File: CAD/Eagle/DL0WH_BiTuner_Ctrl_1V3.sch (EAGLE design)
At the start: 157 parts, among them Q0321 ABS07-32.768KHZ, U0101 STM32L476RXT_64PIN_LDO, U0601 MC33996, U0701 MC33996, U0801 MC33996, U0921 TS5A23166, U0941 LM2611, U0951 OPA354, U0961 OPA354, U0962 MCP4661-103E-MS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

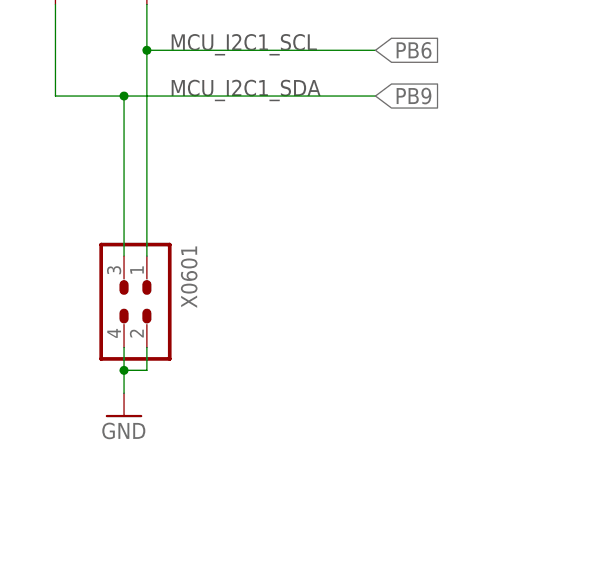
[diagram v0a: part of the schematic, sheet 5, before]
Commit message: HW_1V3 - CAD/Eagle - Rename X0601 to X0501
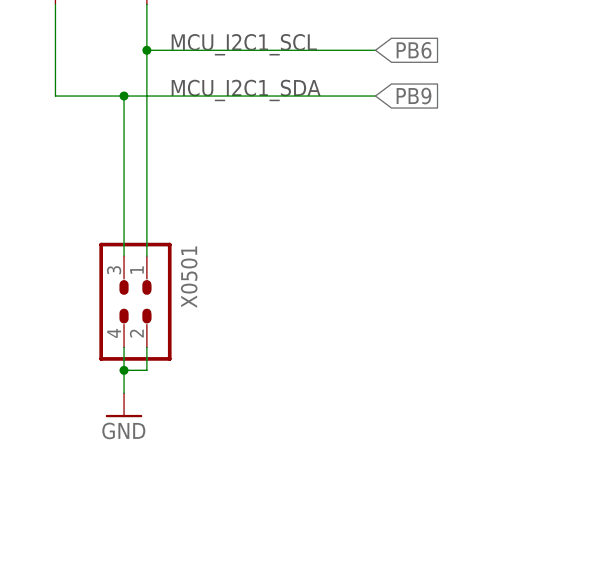
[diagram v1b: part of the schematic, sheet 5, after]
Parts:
- renumbered X0601 to X0501
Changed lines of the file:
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@@
 <part name="R0971" library="df4iah_rcl" deviceset="R-EU_" device="R0402" value="10kR"/>
 <part name="GND0961" library="df4iah_supply" deviceset="GND" device=""/>
-<part name="X0601" library="df4iah_connector" deviceset="HEADER-2X2" device=""/>
+<part name="X0501" library="df4iah_connector" deviceset="HEADER-2X2" device=""/>
 <part name="GND0501" library="df4iah_supply" deviceset="GND" device=""/>
 <part name="+3V6" library="df4iah_supply" deviceset="+3V3" device=""/>
@@
 <instance part="R0511" gate="G$1" x="22.86" y="134.62" rot="R90"/>
 <instance part="R0512" gate="G$1" x="33.02" y="134.62" rot="R90"/>
-<instance part="X0601" gate="G$1" x="33.02" y="96.52" rot="R270"/>
+<instance part="X0501" gate="G$1" x="33.02" y="96.52" rot="R270"/>
 <instance part="GND0501" gate="1" x="30.48" y="83.82"/>
 </instances>
@@
 <pinref part="R0512" gate="G$1" pin="1"/>
 <wire x1="33.02" y1="124.46" x2="33.02" y2="129.54" width="0.1524" layer="91"/>
-<pinref part="X0601" gate="G$1" pin="1"/>
+<pinref part="X0501" gate="G$1" pin="1"/>
 <wire x1="33.02" y1="124.46" x2="33.02" y2="101.6" width="0.1524" layer="91"/>
 <junction x="33.02" y="124.46"/>
@@
 <wire x1="30.48" y1="119.38" x2="58.42" y2="119.38" width="0.1524" layer="91"/>
 <wire x1="22.86" y1="119.38" x2="22.86" y2="129.54" width="0.1524" layer="91"/>
-<pinref part="X0601" gate="G$1" pin="3"/>
+<pinref part="X0501" gate="G$1" pin="3"/>
 <wire x1="30.48" y1="119.38" x2="30.48" y2="101.6" width="0.1524" layer="91"/>
 <junction x="30.48" y="119.38"/>
@@
 <net name="GND" class="0">
 <segment>
-<pinref part="X0601" gate="G$1" pin="2"/>
+<pinref part="X0501" gate="G$1" pin="2"/>
 <wire x1="33.02" y1="91.44" x2="33.02" y2="88.9" width="0.1524" layer="91"/>
-<pinref part="X0601" gate="G$1" pin="4"/>
+<pinref part="X0501" gate="G$1" pin="4"/>
 <wire x1="30.48" y1="91.44" x2="30.48" y2="88.9" width="0.1524" layer="91"/>
 <wire x1="33.02" y1="88.9" x2="30.48" y2="88.9" width="0.1524" layer="91"/>

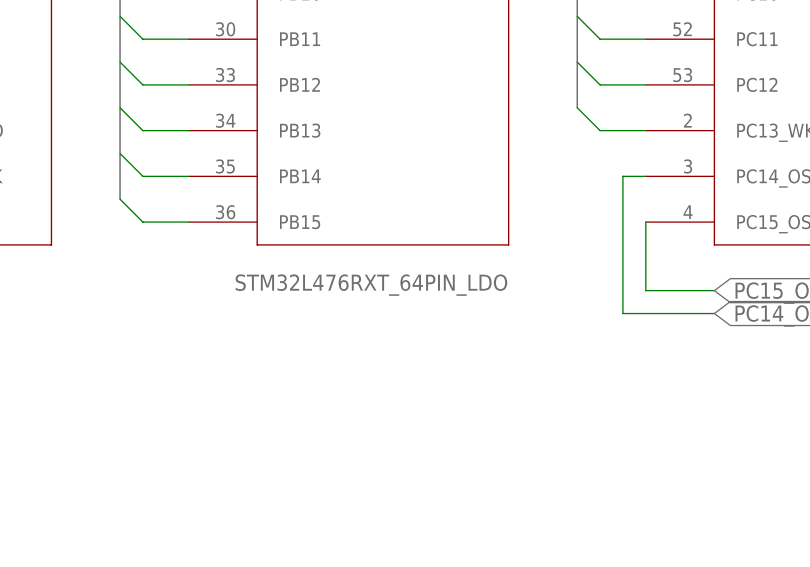
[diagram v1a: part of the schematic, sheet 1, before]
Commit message: HW_1V3 - CAD/Eagle - MCU name fixed
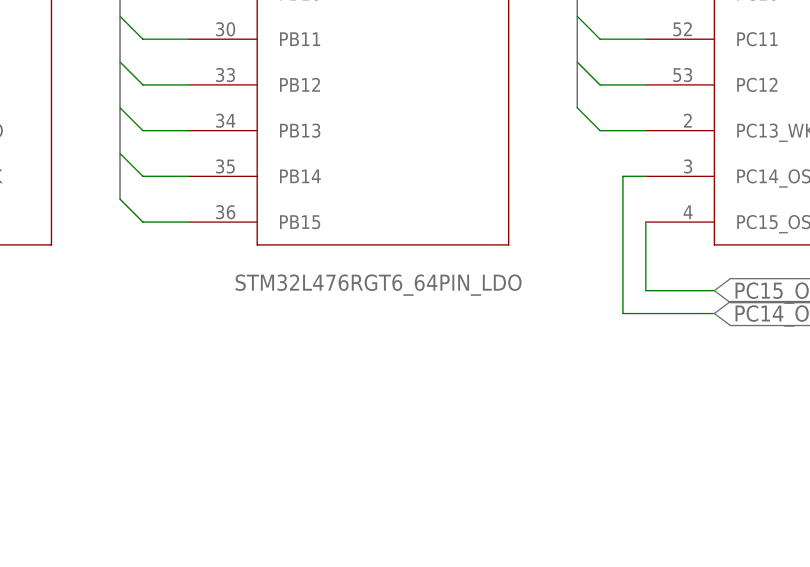
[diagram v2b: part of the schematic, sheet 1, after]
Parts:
- U0101: value STM32L476RXT_64PIN_LDO -> STM32L476RGT6_64PIN_LDO
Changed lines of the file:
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@@
 <part name="C1223" library="df4iah_rcl" deviceset="C-EU" device="C0603" value="22uF"/>
 <part name="X1211" library="df4iah_connector" deviceset="WIRE-TO-BOARD_5MM08_1X02" device=""/>
-<part name="U0101" library="df4iah_stm32l4" deviceset="STM32L476RXT_64PIN_LDO" device=""/>
+<part name="U0101" library="df4iah_stm32l4" deviceset="STM32L476RXT_64PIN_LDO" device="" value="STM32L476RGT6_64PIN_LDO"/>
 <part name="FRAME_07" library="df4iah_frame" deviceset="A4L-LOC" device="" value="Holes"/>
 <part name="FRAME_08" library="df4iah_frame" deviceset="A4L-LOC" device="" value="Holes"/>

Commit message: HW_1V3 - CAD/Eagle - renaming fix, jumper replaced by 0R bridge
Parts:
- removed C0054: 10nF, df4iah_rcl:C-EUC0603
- removed SJ0401: (no value), df4iah_jumper:SJ
- added C1054: 10nF, df4iah_rcl:C-EUC0402
- added R0401: 0R, df4iah_rcl:R-EU_R0402
- C0942: device df4iah_rcl:C-EUC0805 -> df4iah_rcl:C-EUC0603
- C1051, C1052, C1053, C1151, C1152, C1153, C1154: device df4iah_rcl:C-EUC0603 -> df4iah_rcl:C-EUC0402
- R0962: value 1.0kR -> 1kR
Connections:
- net +3V3: now also R0401.1; no longer SJ0401.1
- net GND: now also C1054.2; no longer C0054.2
- net MCU_VDD: now also R0401.2; no longer SJ0401.2
- net RS_DTE_RTR: now also C1054.1; no longer C0054.1
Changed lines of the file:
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@@
 <part name="C0412" library="df4iah_rcl" deviceset="C-EU" device="C0402" value="10nF"/>
 <part name="GND0411" library="df4iah_supply" deviceset="GND" device=""/>
-<part name="SJ0401" library="df4iah_jumper" deviceset="SJ" device=""/>
+<part name="R0401" library="df4iah_rcl" deviceset="R-EU_" device="R0402" value="0R"/>
 <part name="GND0201" library="df4iah_supply" deviceset="GND" device=""/>
 <part name="X0222" library="df4iah_connector" deviceset="HEADER-1X2" device=""/>
@@
 <part name="R0901" library="df4iah_rcl" deviceset="R-EU_" device="R0402" value="1kR"/>
 <part name="R0911" library="df4iah_rcl" deviceset="R-EU_" device="R0402" value="1kR"/>
-<part name="C1052" library="df4iah_rcl" deviceset="C-EU" device="C0603" value="10nF"/>
-<part name="C1051" library="df4iah_rcl" deviceset="C-EU" device="C0603" value="10nF"/>
-<part name="C1053" library="df4iah_rcl" deviceset="C-EU" device="C0603" value="10nF"/>
-<part name="C0054" library="df4iah_rcl" deviceset="C-EU" device="C0603" value="10nF"/>
+<part name="C1052" library="df4iah_rcl" deviceset="C-EU" device="C0402" value="10nF"/>
+<part name="C1051" library="df4iah_rcl" deviceset="C-EU" device="C0402" value="10nF"/>
+<part name="C1053" library="df4iah_rcl" deviceset="C-EU" device="C0402" value="10nF"/>
+<part name="C1054" library="df4iah_rcl" deviceset="C-EU" device="C0402" value="10nF"/>
 <part name="GND0001" library="df4iah_supply" deviceset="GND" device=""/>
 <part name="GND0002" library="df4iah_supply" deviceset="GND" device=""/>
-<part name="C1152" library="df4iah_rcl" deviceset="C-EU" device="C0603" value="10nF"/>
-<part name="C1151" library="df4iah_rcl" deviceset="C-EU" device="C0603" value="10nF"/>
-<part name="C1153" library="df4iah_rcl" deviceset="C-EU" device="C0603" value="10nF"/>
-<part name="C1154" library="df4iah_rcl" deviceset="C-EU" device="C0603" value="10nF"/>
+<part name="C1152" library="df4iah_rcl" deviceset="C-EU" device="C0402" value="10nF"/>
+<part name="C1151" library="df4iah_rcl" deviceset="C-EU" device="C0402" value="10nF"/>
+<part name="C1153" library="df4iah_rcl" deviceset="C-EU" device="C0402" value="10nF"/>
+<part name="C1154" library="df4iah_rcl" deviceset="C-EU" device="C0402" value="10nF"/>
 <part name="GND0005" library="df4iah_supply" deviceset="GND" device=""/>
 <part name="GND0006" library="df4iah_supply" deviceset="GND" device=""/>
@@
 <part name="U0961" library="df4iah_opamp" deviceset="OPA354" device=""/>
 <part name="R0961" library="df4iah_rcl" deviceset="R-EU_" device="R0402" value="1kR"/>
-<part name="R0962" library="df4iah_rcl" deviceset="R-EU_" device="R0402" value="1.0kR"/>
+<part name="R0962" library="df4iah_rcl" deviceset="R-EU_" device="R0402" value="1kR"/>
 <part name="R0963" library="df4iah_rcl" deviceset="R-EU_" device="R0402" value="10kR"/>
 <part name="C0963" library="df4iah_rcl" deviceset="C-EU" device="C0402" value="100pF"/>
@@
 <part name="GND0941" library="df4iah_supply" deviceset="GND" device=""/>
 <part name="L0941" library="df4iah_rcl" deviceset="L-EU" device="L1812" value="20uH"/>
-<part name="C0942" library="df4iah_rcl" deviceset="C-EU" device="C0805" value="2.2uF"/>
+<part name="C0942" library="df4iah_rcl" deviceset="C-EU" device="C0603" value="2.2uF"/>
 <part name="GND0942" library="df4iah_supply" deviceset="GND" device=""/>
 <part name="L0943" library="df4iah_rcl" deviceset="L-EU" device="L1812" value="20uH"/>
@@
 <instance part="C0412" gate="G$1" x="200.66" y="101.6"/>
 <instance part="GND0411" gate="1" x="200.66" y="88.9"/>
-<instance part="SJ0401" gate="1" x="119.38" y="147.32"/>
+<instance part="R0401" gate="G$1" x="119.38" y="147.32"/>
 <instance part="GND0441" gate="1" x="200.66" y="33.02"/>
 <instance part="R0441" gate="G$1" x="213.36" y="38.1"/>
@@
 <wire x1="165.1" y1="147.32" x2="165.1" y2="139.7" width="0.1524" layer="91"/>
 <junction x="165.1" y="147.32"/>
-<pinref part="SJ0401" gate="1" pin="2"/>
+<pinref part="R0401" gate="G$1" pin="2"/>
 <wire x1="134.62" y1="147.32" x2="124.46" y2="147.32" width="0.1524" layer="91"/>
 <pinref part="C0410" gate="G$1" pin="1"/>
@@
 <net name="+3V3" class="0">
 <segment>
-<pinref part="SJ0401" gate="1" pin="1"/>
+<pinref part="R0401" gate="G$1" pin="1"/>
 <label x="40.64" y="147.32" size="1.778" layer="95" rot="R180" xref="yes"/>
 <wire x1="114.3" y1="147.32" x2="40.64" y2="147.32" width="0.1524" layer="91"/>
@@
 <instance part="C1051" gate="G$1" x="180.34" y="114.3"/>
 <instance part="C1053" gate="G$1" x="180.34" y="81.28"/>
-<instance part="C0054" gate="G$1" x="193.04" y="81.28"/>
+<instance part="C1054" gate="G$1" x="193.04" y="81.28"/>
 <instance part="GND0001" gate="1" x="180.34" y="106.68"/>
 <instance part="GND0002" gate="1" x="180.34" y="73.66"/>
@@
 <wire x1="180.34" y1="76.2" x2="193.04" y2="76.2" width="0.1524" layer="91"/>
 <junction x="180.34" y="76.2"/>
-<pinref part="C0054" gate="G$1" pin="2"/>
+<pinref part="C1054" gate="G$1" pin="2"/>
 </segment>
 </net>
@@
 <pinref part="X1053" gate="G$1" pin="2"/>
 <wire x1="165.1" y1="88.9" x2="193.04" y2="88.9" width="0.1524" layer="91"/>
-<pinref part="C0054" gate="G$1" pin="1"/>
+<pinref part="C1054" gate="G$1" pin="1"/>
 <wire x1="193.04" y1="88.9" x2="215.9" y2="88.9" width="0.1524" layer="91"/>
 <wire x1="193.04" y1="88.9" x2="193.04" y2="83.82" width="0.1524" layer="91"/>

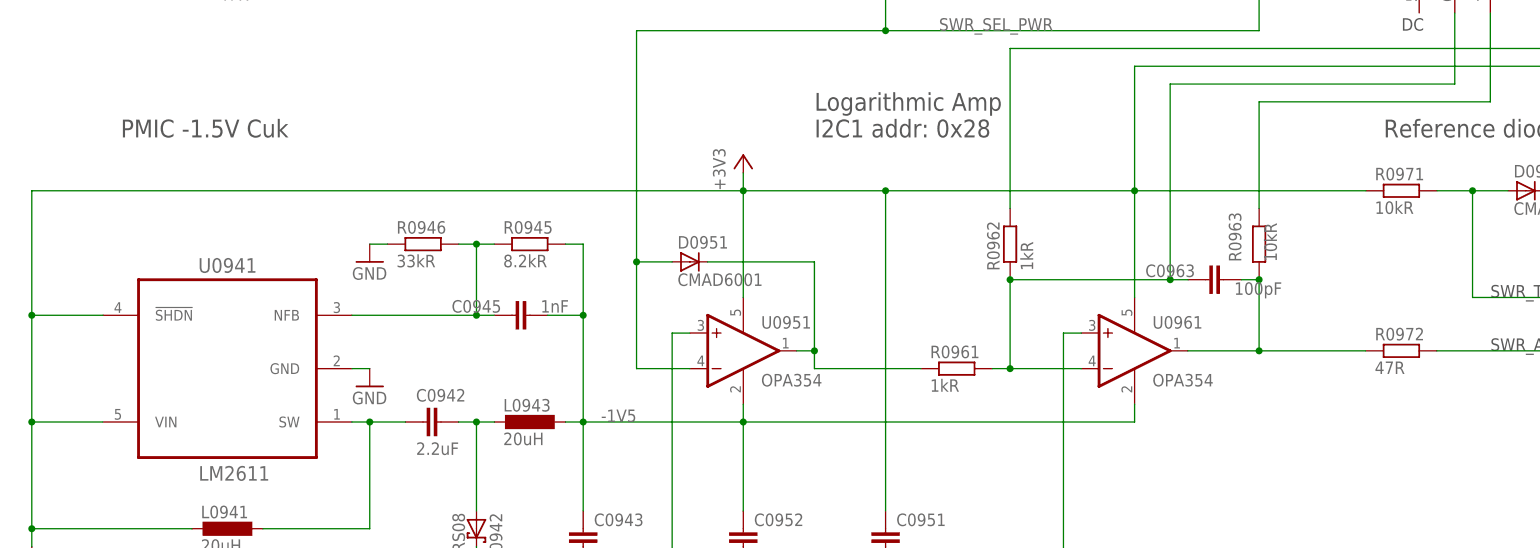
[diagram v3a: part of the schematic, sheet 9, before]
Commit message: HW_1V3 - CAD/Eagle - PMIC CUK additional soft-start, OpAmp output w/ higher resistor
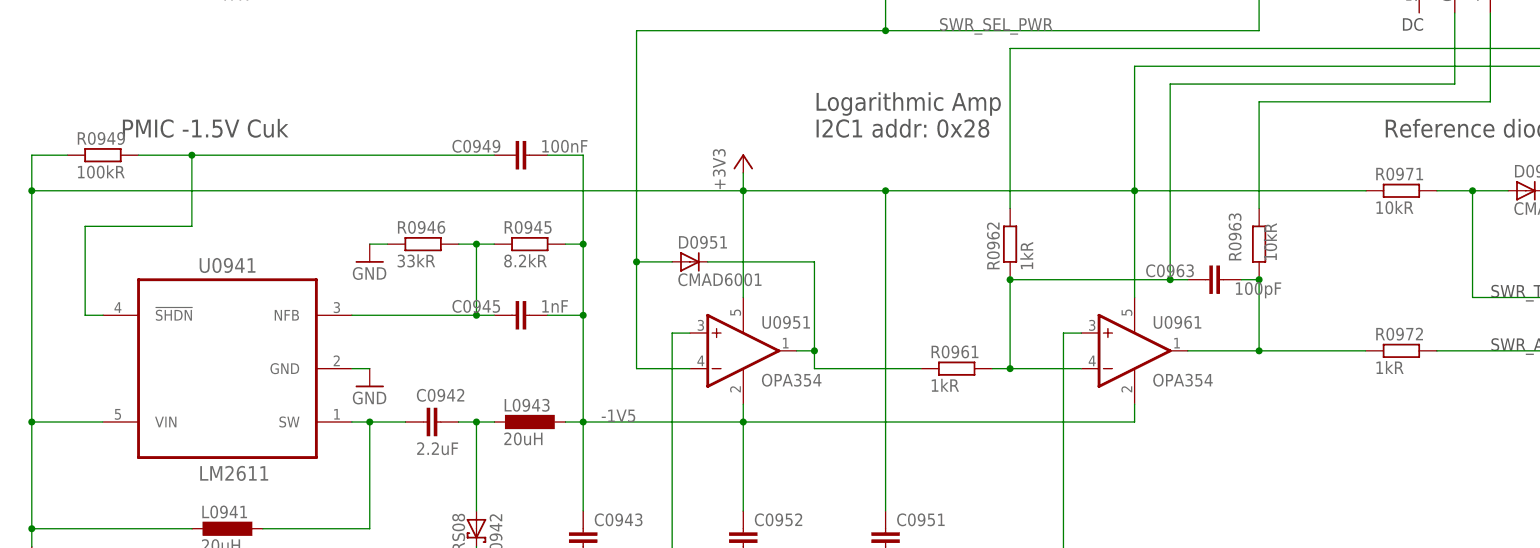
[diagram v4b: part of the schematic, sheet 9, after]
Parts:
- added C0949: 100nF, df4iah_rcl:C-EUC0402
- added R0949: 100kR, df4iah_rcl:R-EU_R0402
- R0972: value 47R -> 1kR
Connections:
- new net LM_SHDN: C0949.1, R0949.2, U0941.!SHDN
- net +3V3: now also R0949.1; no longer U0941.!SHDN
- net -1V5: now also C0949.2
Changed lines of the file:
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@@
 <part name="C0951" library="df4iah_rcl" deviceset="C-EU" device="C0402" value="100nF"/>
 <part name="D0951" library="df4iah_diode" deviceset="D_SOD923" device="" value="CMAD6001"/>
-<part name="R0972" library="df4iah_rcl" deviceset="R-EU_" device="R0402" value="47R"/>
+<part name="R0972" library="df4iah_rcl" deviceset="R-EU_" device="R0402" value="1kR"/>
 <part name="D0971" library="df4iah_diode" deviceset="D_SOD923" device="" value="CMAD6001"/>
 <part name="R0971" library="df4iah_rcl" deviceset="R-EU_" device="R0402" value="10kR"/>
@@
 <part name="+3V7" library="df4iah_supply" deviceset="+3V3" device=""/>
 <part name="C0962" library="df4iah_rcl" deviceset="C-EU" device="C0402" value="100nF"/>
+<part name="C0949" library="df4iah_rcl" deviceset="C-EU" device="C0402" value="100nF"/>
+<part name="R0949" library="df4iah_rcl" deviceset="R-EU_" device="R0402" value="100kR"/>
 </parts>
 <sheets>
@@
 <instance part="+3V7" gate="G$1" x="246.38" y="167.64"/>
 <instance part="C0962" gate="G$1" x="238.76" y="147.32"/>
+<instance part="C0949" gate="G$1" x="78.74" y="76.2" smashed="yes" rot="R90">
+<attribute name="NAME" x="70.104" y="76.581" size="1.778" layer="95"/>
+<attribute name="VALUE" x="82.804" y="76.581" size="1.778" layer="96"/>
+</instance>
+<instance part="R0949" gate="G$1" x="20.32" y="76.2"/>
 </instances>
 <busses>
@@
 <pinref part="U0941" gate="G$1" pin="VIN"/>
 <wire x1="20.32" y1="38.1" x2="10.16" y2="38.1" width="0.1524" layer="91"/>
-<wire x1="10.16" y1="38.1" x2="10.16" y2="53.34" width="0.1524" layer="91"/>
-<pinref part="U0941" gate="G$1" pin="!SHDN"/>
-<wire x1="10.16" y1="53.34" x2="20.32" y2="53.34" width="0.1524" layer="91"/>
-<wire x1="10.16" y1="71.12" x2="10.16" y2="53.34" width="0.1524" layer="91"/>
-<junction x="10.16" y="53.34"/>
+<wire x1="10.16" y1="71.12" x2="10.16" y2="38.1" width="0.1524" layer="91"/>
 <pinref part="C0941" gate="G$1" pin="1"/>
 <wire x1="10.16" y1="38.1" x2="10.16" y2="22.86" width="0.1524" layer="91"/>
@@
 <pinref part="U0962" gate="G$1" pin="P0A"/>
 <wire x1="238.76" y1="88.9" x2="238.76" y2="96.52" width="0.1524" layer="91"/>
+<wire x1="10.16" y1="71.12" x2="10.16" y2="76.2" width="0.1524" layer="91"/>
+<junction x="10.16" y="71.12"/>
+<pinref part="R0949" gate="G$1" pin="1"/>
+<wire x1="10.16" y1="76.2" x2="15.24" y2="76.2" width="0.1524" layer="91"/>
 </segment>
 <segment>
@@
 <wire x1="88.9" y1="53.34" x2="83.82" y2="53.34" width="0.1524" layer="91"/>
 <junction x="88.9" y="53.34"/>
+<wire x1="88.9" y1="63.5" x2="88.9" y2="76.2" width="0.1524" layer="91"/>
+<junction x="88.9" y="63.5"/>
+<pinref part="C0949" gate="G$1" pin="2"/>
+<wire x1="88.9" y1="76.2" x2="83.82" y2="76.2" width="0.1524" layer="91"/>
 </segment>
 </net>
@@
 </segment>
 </net>
+<net name="LM_SHDN" class="0">
+<segment>
+<pinref part="U0941" gate="G$1" pin="!SHDN"/>
+<wire x1="20.32" y1="53.34" x2="17.78" y2="53.34" width="0.1524" layer="91"/>
+<wire x1="17.78" y1="53.34" x2="17.78" y2="66.04" width="0.1524" layer="91"/>
+<wire x1="17.78" y1="66.04" x2="33.02" y2="66.04" width="0.1524" layer="91"/>
+<wire x1="33.02" y1="66.04" x2="33.02" y2="76.2" width="0.1524" layer="91"/>
+<pinref part="R0949" gate="G$1" pin="2"/>
+<wire x1="33.02" y1="76.2" x2="25.4" y2="76.2" width="0.1524" layer="91"/>
+<pinref part="C0949" gate="G$1" pin="1"/>
+<wire x1="33.02" y1="76.2" x2="76.2" y2="76.2" width="0.1524" layer="91"/>
+<junction x="33.02" y="76.2"/>
+</segment>
+</net>
